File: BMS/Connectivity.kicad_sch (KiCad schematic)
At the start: 46 parts, among them J10 Conn_01x06, J11 Conn_01x06, J17 Conn_01x04, J2 Conn_01x02, J3 Conn_01x02, J4 Conn_01x02, J7 FTSH-107-01-L-D-K, J8 Conn_01x02, J9 Conn_01x06, Q4 DMT6018LDR-7, Q5 DMT6018LDR-7, SW1 SW_Push, U4 MCP2542FD-E/MF

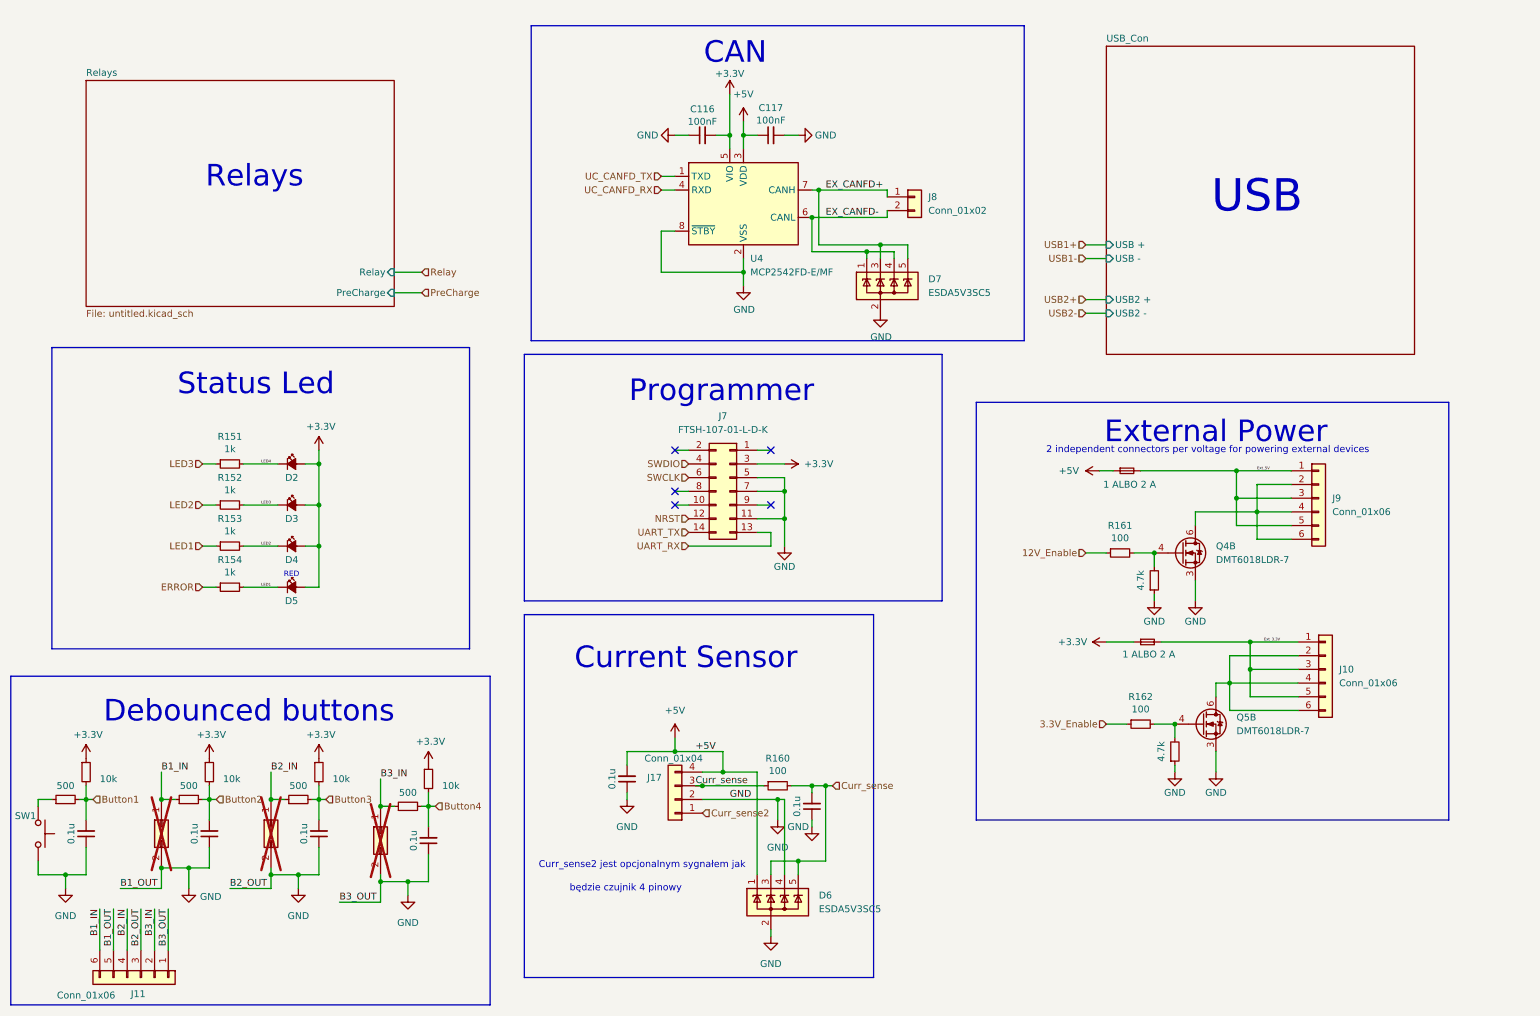
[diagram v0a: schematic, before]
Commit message: Dodano layout drugiego bq79614, ukladu tlumaczącego z protokułu TI na UART oraz wstępnie poprowadzono pary różnicowe
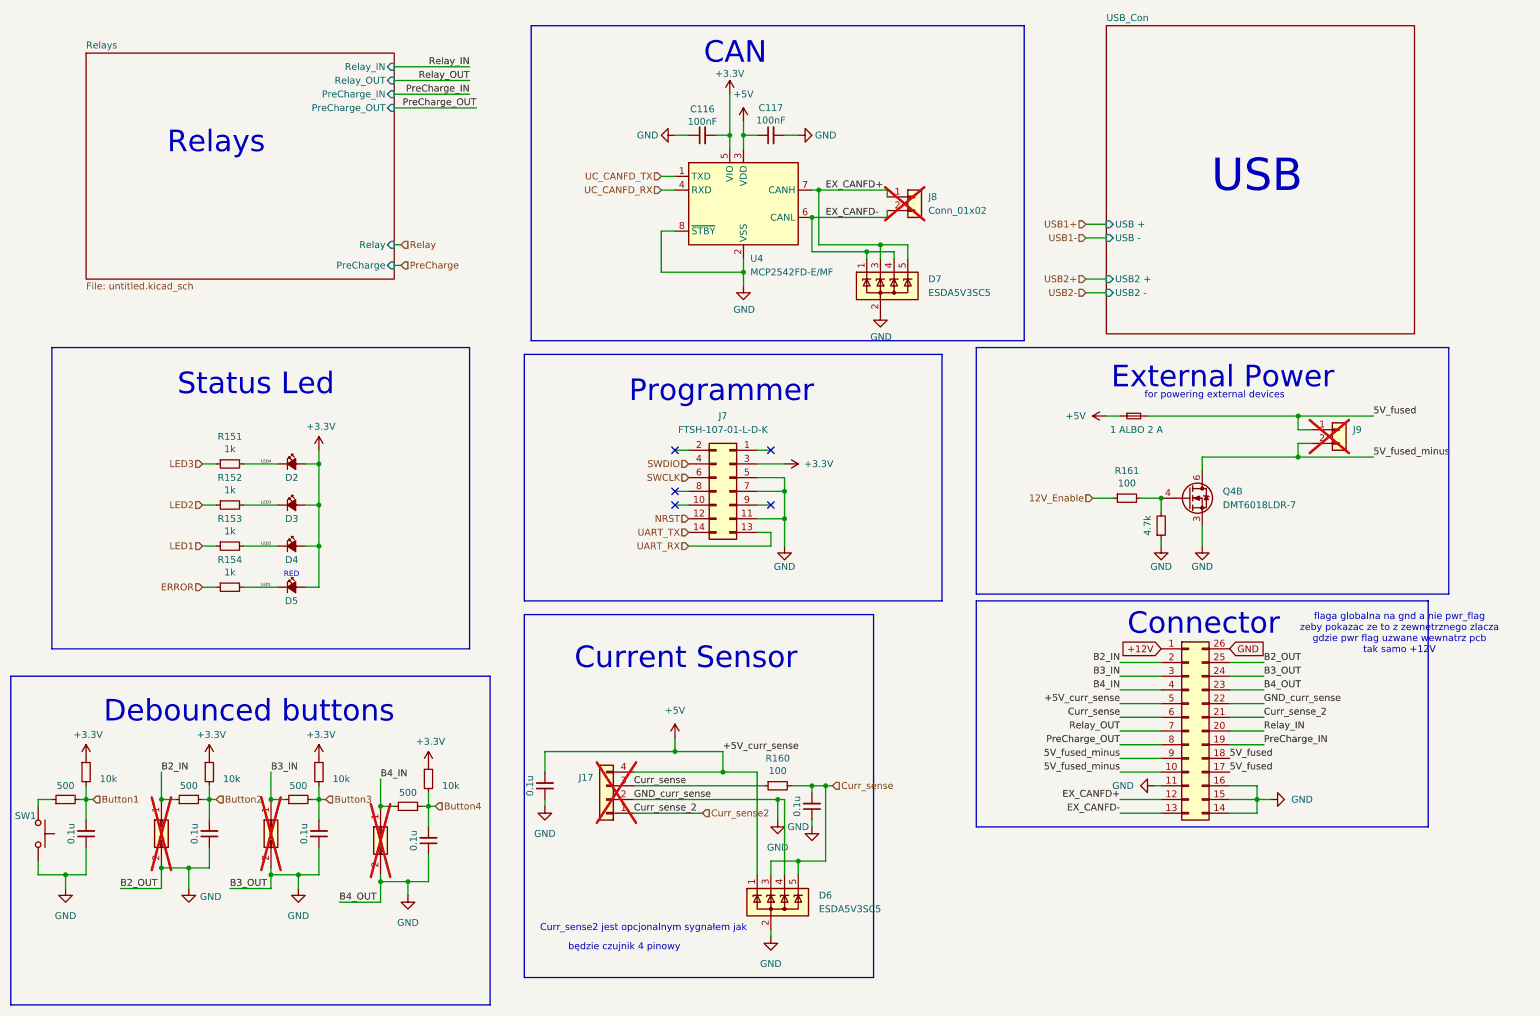
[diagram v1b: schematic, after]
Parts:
- removed F2: 1 ALBO 2 A, Resistor_SMD:R_0402_1005Metric_Pad0.72x0.64mm_HandSolder, symbol Device:Fuse_Small
- removed J10, J11, J9: Conn_01x06, footrpint:HARWIN_M300-MV30645M1, symbol Connector_Generic:Conn_01x06
- removed Q5: DMT6018LDR-7, Samacsys:DMT6018LDR7, symbol Samacsys_kicad_sym:DMT6018LDR-7
- removed R162: 100, Resistor_SMD:R_0603_1608Metric, symbol Device:R_Small
- removed R164: 4.7k, Resistor_SMD:R_0603_1608Metric, symbol Device:R_Small
- added J19: Conn_02x13_Counter_Clockwise, footrpint:HARWIN_M80-5402642, symbol Connector_Generic:Conn_02x13_Counter_Clockwise
- added J9: Conn_01x02, footrpint:HARWIN_M55-3100242R, symbol Connector_Generic:Conn_01x02
- J17, J8: now not fitted; now left out of the parts list
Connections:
- net B1_IN is gone; now on net B2_IN: J2.1 (Pin_1), R149.1
- net +5V: no longer C115.2, D6.1 (K), J17.4 (Pin_4)
- net B2_IN: now also J19.2 (Pin_2); no longer J3.1 (Pin_1), R156.1
- net B3_IN: now also J3.1 (Pin_1), R156.1, J19.3 (Pin_3); no longer J4.1 (Pin_1), R158.1
- net Curr_sense: now also J19.6 (Pin_6)
- net Curr_sense2: now also J19.21 (Pin_21)
- net EX_CANFD+: now also J19.12 (Pin_12)
- net EX_CANFD-: now also J19.13 (Pin_13)
- net GND: now also J19.11 (Pin_11), J19.14 (Pin_14), J19.15 (Pin_15), J19.16 (Pin_16), J19.22 (Pin_22), J19.23 (Pin_23), J19.24 (Pin_24), J19.25 (Pin_25), J19.26 (Pin_26)
- net 5V_fused_minus: now reaches Q4.6 (D2)
- net 5V_fused_minus: now also J19.10 (Pin_10), J19.9 (Pin_9), J9.2 (Pin_2)
- net Ext_5V renamed 5V_fused
- net 5V_fused: now also J19.17 (Pin_17), J19.18 (Pin_18), J9.1 (Pin_1)
- new net +12V: J19.1 (Pin_1)
- new net +5V_curr_sense: C115.2, D6.1 (K), J17.4 (Pin_4), J19.5 (Pin_5)
- new net B4_IN: J19.4 (Pin_4), J4.1 (Pin_1), R158.1
- new net PreCharge_IN: J19.19 (Pin_19)
- new net PreCharge_OUT: J19.8 (Pin_8)
- new net Relay_IN: J19.20 (Pin_20)
- new net Relay_OUT: J19.7 (Pin_7)
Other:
- sheet Relays ports: added PreCharge_IN, PreCharge_OUT, Relay_IN, Relay_OUT; removed none
- note added: "Connector"
- note added: "flaga globalna na gnd a nie pwr_flag zeby pokazac ze to z zewnetrznego zlacza gdzie pwr flag uzwane wewnatrz pcb tak samo +12V"
- note added: "for powering external devices"
- note removed: "2 independent connectors per voltage for powering external devices"
- moved on the sheet: Q4B, R161

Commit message: Iteracja 1.0 gotowa, teraz sprawdzenie i zmiany kosmetyczne
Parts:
- added D1, D13: 60V/0.5/3A, Diode_SMD:D_SOD-123, symbol Device:D_Schottky_Small
- added D11, D12: ESDA5V3SC5, Package_TO_SOT_SMD:SOT-23-5, symbol Power_Protection:ESDA5V3SC5
- added J11: USB4235-03-C_REVA, footrpint:GCT_USB4235-03-C_REVA, symbol USB4235-03-C_REVA:USB4235-03-C_REVA
- added J13: USB_A, footrpint:USB1046GF0190LBA, symbol Connector:USB_A
- added J5, J6: ~, footrpint:HARWIN_M80-5000000M1-02-PM1-00-000, symbol Connector:Conn_01x02_Socket
- added JP1: Jumper_2_Small_Open, Jumper:SolderJumper-2_P1.3mm_Open_Pad1.0x1.5mm, symbol Jumper:Jumper_2_Small_Open
- added Q3, Q6: DMT6018LDR-7, Samacsys:DMT6018LDR7, symbol Samacsys_kicad_sym:DMT6018LDR-7
- added Q5, Q7: DMT6018LDR-7, DMT6018LDR7, symbol DMT6018LDR-7:DMT6018LDR-7
- added R173, R174, R175, R176: 33, Resistor_SMD:R_0603_1608Metric, symbol Device:R_Small
- added R3, R58: 100, Resistor_SMD:R_0603_1608Metric, symbol Device:R_Small
- added R56, R59: 10k, Resistor_SMD:R_0603_1608Metric, symbol Device:R_Small
- added R75, R76: 5.1K, Resistor_SMD:R_0603_1608Metric, symbol Device:R_Small
- added TP1, TP10, TP11, TP17, TP18, TP2, TP3, TP4, TP5, TP6, TP7, TP8, TP9: TestPoint_Small, TestPoint:TestPoint_Pad_D1.0mm, symbol Connector:TestPoint_Small
- C110, C111, C112, C114, C115, C116, C117, C118: footprint Capacitor_SMD:C_0603_1608Metric -> Capacitor_SMD:C_0603_1608Metric_Pad1.08x0.95mm_HandSolder
- F1: value 1 ALBO 2 A -> 3A; footprint Resistor_SMD:R_0402_1005Metric_Pad0.72x0.64mm_HandSolder -> Fuse:Fuse_0603_1608Metric_Pad1.05x0.95mm_HandSolder
- Q4: now not fitted; now left out of the parts list
- R151, R152, R153, R154, R160, R161, R163: footprint Resistor_SMD:R_0603_1608Metric -> Resistor_SMD:R_0603_1608Metric_Pad0.98x0.95mm_HandSolder
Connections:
- net PreCharge_IN is gone; now on net Curr_sense2: J19.19 (Pin_19)
- net PreCharge_OUT is gone; now on net 5V_fused_minus: J19.8 (Pin_8)
- net Relay_IN is gone; now on net GND: J19.20 (Pin_20)
- net Relay_OUT is gone; now on net 5V_fused_minus: J19.7 (Pin_7)
- net +12V: now also J19.3 (Pin_3), J19.4 (Pin_4), D1.1 (K), D13.1 (K), J5.1 (Pin_1), J6.1 (Pin_1)
- net +5V_curr_sense: now also J19.2 (Pin_2); no longer J19.5 (Pin_5)
- net 12V_Enable: now also TP1.1
- net 5V_fused: now also J19.10 (Pin_10), J19.9 (Pin_9), TP17.1; no longer J19.17 (Pin_17), J19.18 (Pin_18)
- net 5V_fused_minus: now also Q7.5 (D1), TP18.1; no longer J19.10 (Pin_10), J19.9 (Pin_9)
- net B2_IN: now also J19.26 (Pin_26); no longer J19.2 (Pin_2)
- net B3_IN: now also J19.24 (Pin_24); no longer J19.3 (Pin_3)
- net B4_IN: now also J19.22 (Pin_22); no longer J19.4 (Pin_4)
- net Button1: now also TP9.1
- net Button2: now also TP6.1
- net Button3: now also TP7.1
- net Button4: now also TP8.1
- net Curr_sense: now also JP1.2 (B); no longer D6.3 (K), J17.3 (Pin_3), J19.6 (Pin_6), R160.1
- net Curr_sense2: now also D6.3 (K), TP5.1; no longer J19.21 (Pin_21)
- net GND: now also J19.17 (Pin_17), J19.21 (Pin_21), D11.2 (A), D12.2 (A), J11.A1 (GND_A), J11.A12 (GND_A), J11.B1 (GND_B), J11.B12 (GND_B), J11.SH1 (SHIELD), J11.SH2 (SHIELD), J13.4 (GND), Q3.3 (S2), Q5.2 (S1), Q5.3 (S2), Q6.3 (S2), Q7.2 (S1), R56.1, R59.1, R75.1, R76.2; no longer J19.11 (Pin_11), J19.22 (Pin_22), J19.24 (Pin_24), J19.26 (Pin_26)
- net LED1: no longer D5.1 (K), R154.2
- net LED2: no longer D4.1 (K), R153.2
- net LED3: no longer D3.1 (K), R152.2
- net PreCharge: now also R58.1
- net Relay: now also R3.1
- net USB1+: now also R176.1
- net USB1-: now also R175.1
- net G3: now reaches Q4.4 (G2), R161.2, R163.2
- net G3: now also Q7.1 (G1)
- net LED4: no longer names the net of D2.1 (K), R151.2
- new net: D3.1 (K), R152.2
- new net: D11.1 (K), D11.5 (K), J13.2 (D-), R174.2
- new net: D11.3 (K), D11.4 (K), J13.3 (D+), R173.2
- new net: D5.1 (K), R154.2
- new net: J11.B5 (CC2), R76.1
- new net: D4.1 (K), R153.2
- new net: J11.A5 (CC1), R75.2
- new net: J11.A4 (VBUS_A), J11.A9 (VBUS_A)
- new net: J11.B4 (VBUS_B), J11.B9 (VBUS_B)
- new net Curr_sense_out: J17.3 (Pin_3), J19.18 (Pin_18), JP1.1 (A), R160.1, TP4.1
- new net D1: D1.2 (A), J19.6 (Pin_6), J5.2 (Pin_2), Q3.6 (D2), Q5.5 (D1), TP10.1
- new net D2: D13.2 (A), J19.5 (Pin_5), J6.2 (Pin_2), Q5.6 (D2), Q6.6 (D2), TP11.1
- new net DP: D12.3 (K), D12.4 (K), J11.A6 (DP1), J11.B7 (DN2), R175.2
- new net G1: Q3.4 (G2), Q5.1 (G1), R3.2, R56.2, TP2.1
- new net G2: Q5.4 (G2), Q6.4 (G2), R58.2, R59.2, TP3.1
- new net NP: D12.1 (K), D12.5 (K), J11.A7 (DN1), J11.B6 (DP2), R176.2
- new net USB2 +: R173.1
- new net USB2 -: R174.1
- new net VBUS: J13.1 (VBUS)
- no-connect marks 5 -> 12
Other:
- removed sheet Relays
- removed sheet USB_Con
- note added: "RELAYS"
- note added: "USB_A"
- note added: "USB_C"
- note added: "symbol stedni, potem zmienie na czytelniejszy"
- note removed: "Relays"
- note removed: "USB"
- note removed: "flaga globalna na gnd a nie pwr_flag zeby pokazac ze to z zewnetrznego zlacza gdzie pwr flag uzwane wewnatrz pcb tak samo +12V"
- title: (none) -> Battery Management System for a high power gokart battery
- moved on the sheet: C116, C117, D2, D3, D4, D5, D6, D7, J17, J8, J9, R151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
